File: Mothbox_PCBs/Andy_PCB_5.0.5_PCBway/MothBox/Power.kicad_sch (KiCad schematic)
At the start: 50 parts, among them J1 DB141V-2.54-4P, J2 DB141V-2.54-4P, J3 DB141V-2.54-4P, Q1 AP30P30Q, Q10 AP30P30Q, Q2 AO3400A, Q8 AP30P30Q, SW2 KH-6X6X5H-STM, U1 Place Holder voltage regulator, U2 XL4015E1, U3 INA219BIDCNT

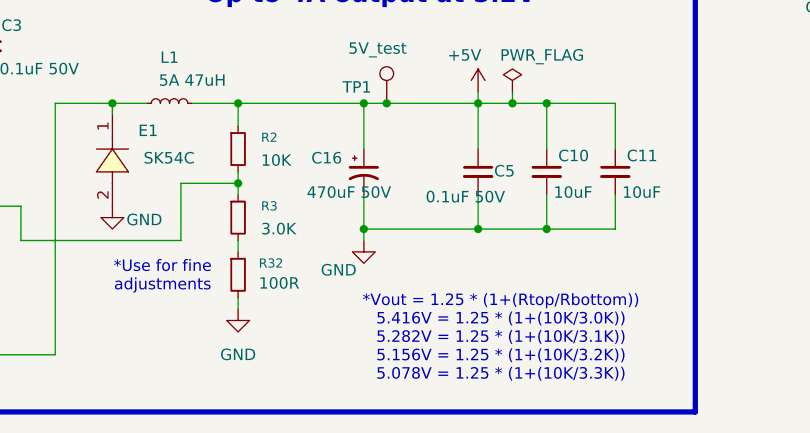
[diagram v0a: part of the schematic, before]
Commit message: tweaked incorrect descriptions for some parts
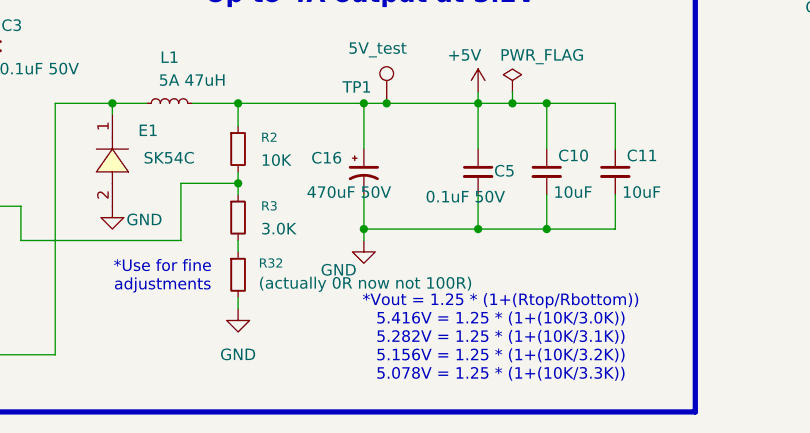
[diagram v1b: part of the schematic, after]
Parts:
- R32: value 100R -> (actually 0R now not 100R)
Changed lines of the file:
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@@
 			)
 		)
-		(property "Value" "100R"
+		(property "Value" "(actually 0R now not 100R)"
 			(at 122.936 158.4299 0)
 			(effects
